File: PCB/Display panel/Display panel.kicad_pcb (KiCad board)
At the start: 2 copper layers, 70 x 36 mm, 13 parts, among them J1 Conn_01x12_MountingPin, J2 IDC, Q2 BSS138, SW2 EC11E18244AU, U1 APX803S-31SA-7

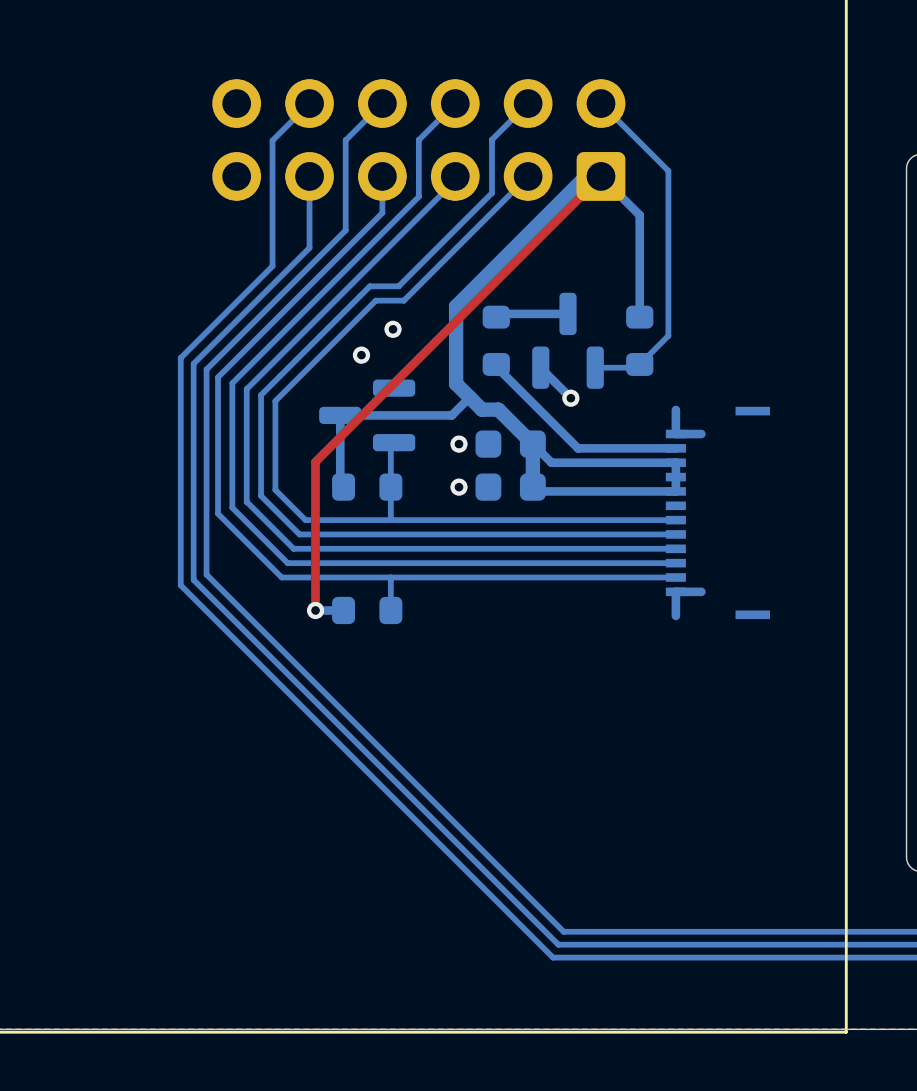
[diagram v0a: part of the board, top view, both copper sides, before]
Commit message: Updated the PCB Allot
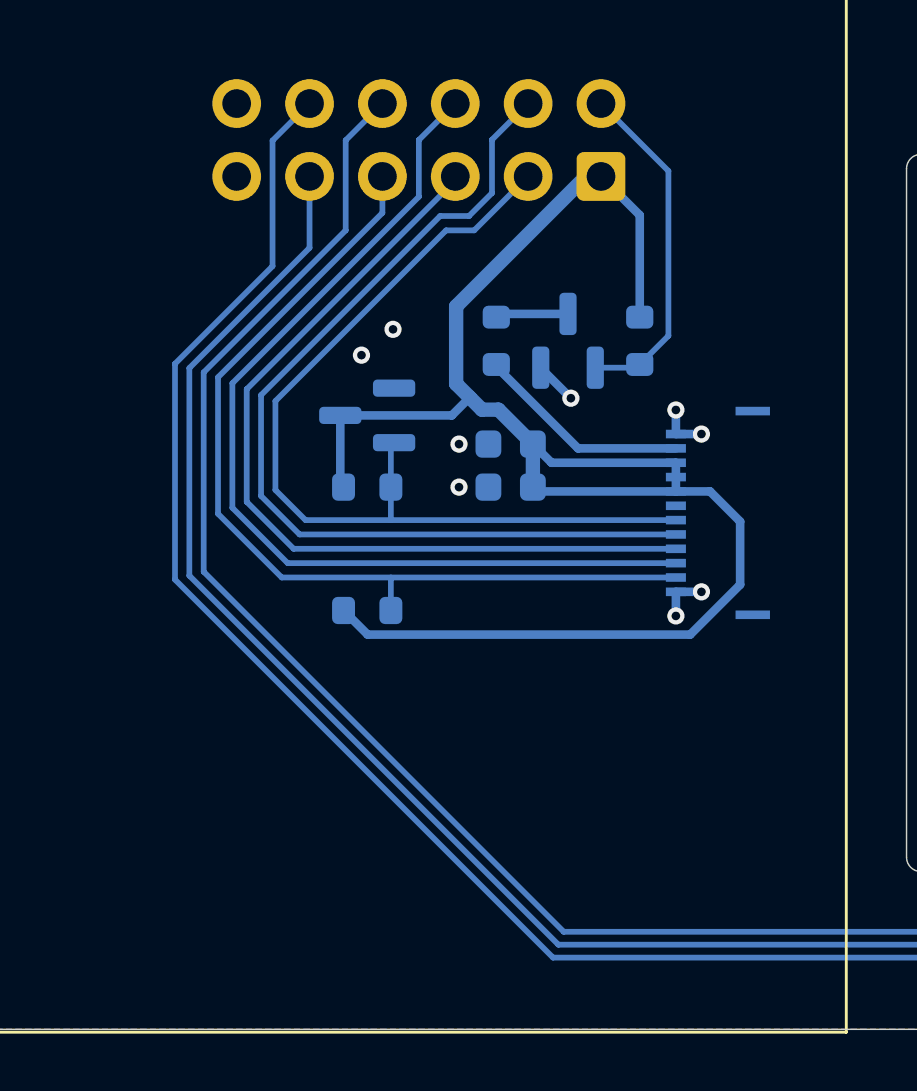
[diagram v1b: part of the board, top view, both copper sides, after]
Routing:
- net +3V3: track 59.0 -> 58.5 mm, vias 1 -> 0
- net GND: vias 5 -> 9
